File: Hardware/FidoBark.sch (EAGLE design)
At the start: 16 parts

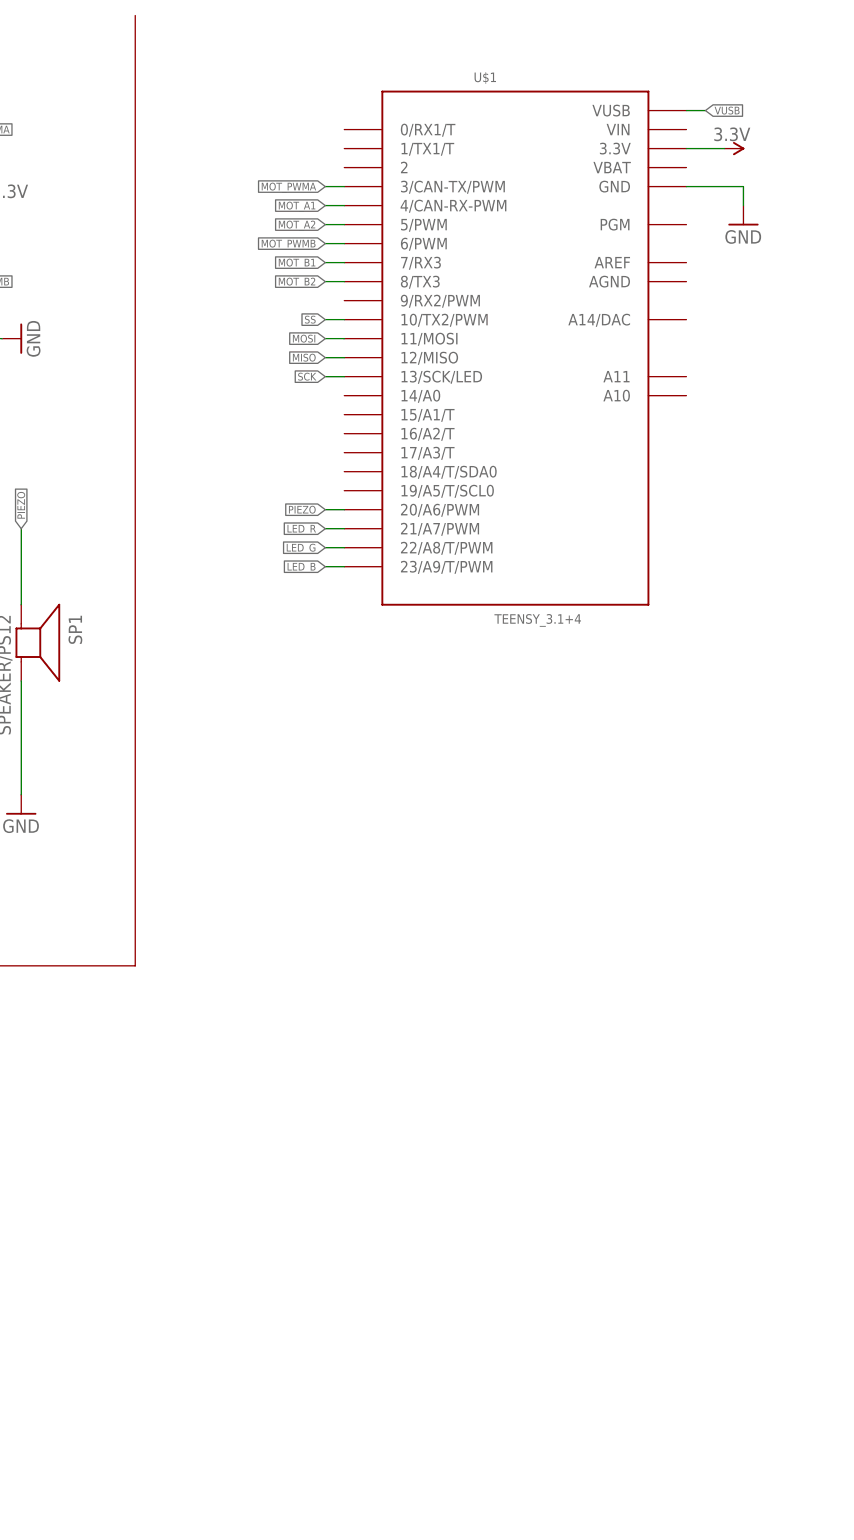
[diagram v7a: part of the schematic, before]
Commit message: added vis/ir light, mice
dat op-amp do
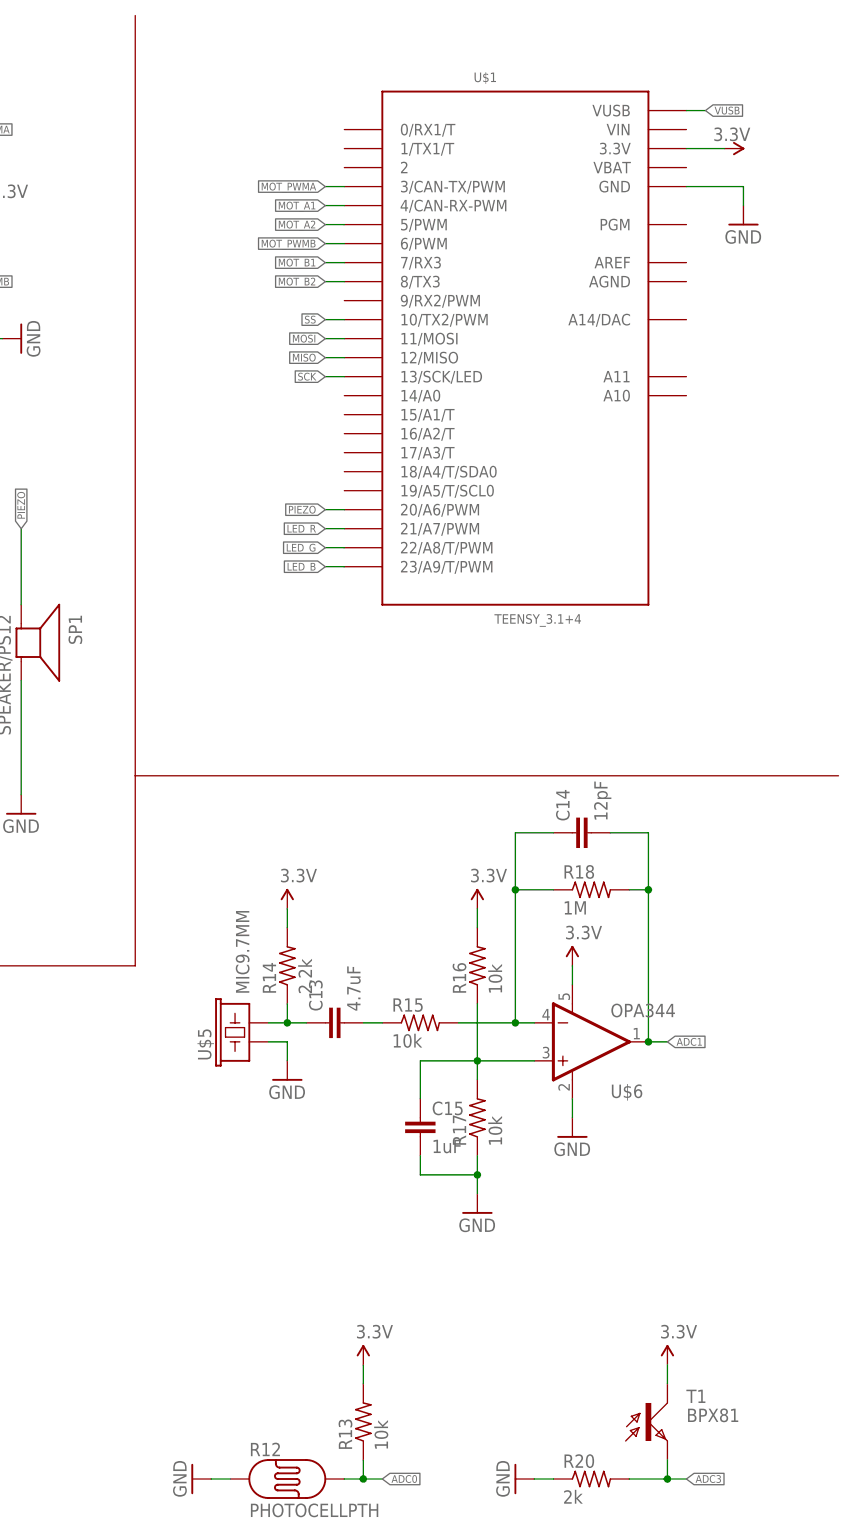
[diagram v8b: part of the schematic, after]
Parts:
- added C13: 4.7uF, SparkFun-Passives:CAP0603-CAP
- added C14: 12pF, SparkFun-Passives:CAP0603-CAP
- added C15: 1uF, SparkFun-Passives:CAP0603-CAP
- added R12: PHOTOCELLPTH, SparkFun-Sensors:PHOTOCELLPTH
- added R13, R15, R16, R17: 10k, adafruit:R-US_R0603
- added R14: 2.2k, adafruit:R-US_R0603
- added R18: 1M, adafruit:R-US_R0603
- added R20: 2k, adafruit:R-US_R0603
- added T1: BPX81, opto-trans-siemens:BPX81
- added U$5: MIC9.7MM, SparkFun-Sensors:MIC9.7MM
- added U$6: OPA344, SparkFun-AnalogIC:OPA344
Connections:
- new net ADC0: R12.P$2, R13.1
- new net ADC1: C14.2, R18.2, U$6.OUT
- new net ADC3: R20.2, T1.E
- new net N$28: C13.1, R14.1, U$5.2
- new net N$29: C13.2, R15.1
- new net N$30: C14.1, R15.2, R18.1, U$6.-IN
- new net N$32: C15.1, R16.1, R17.2, U$6.+IN
- net 3.3V: now also R13.2, R14.2, R16.2, T1.C, U$6.V+
- net GND: now also C15.2, R12.P$1, R17.1, R20.1, U$5.1, U$6.V-
